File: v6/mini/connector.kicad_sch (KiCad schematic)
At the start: 25 parts, among them J1 USB-C Receptable (16P), U1 PAC1954T-E4Mx, U2 ADP7142AUJZ, U3 ADP7142AUJZ

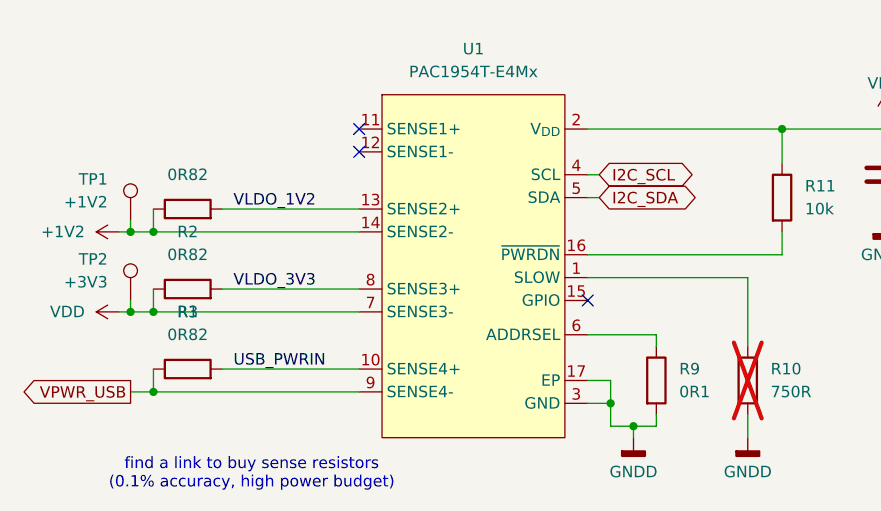
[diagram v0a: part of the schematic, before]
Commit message: Add comments for GateMAte board
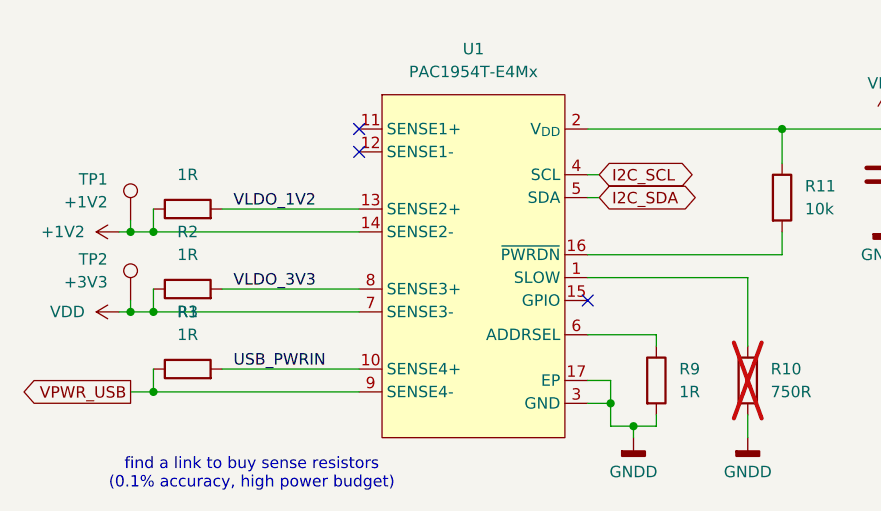
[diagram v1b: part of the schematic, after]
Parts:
- R1, R2, R3: value 0R82 -> 1R
- R9: value 0R1 -> 1R
